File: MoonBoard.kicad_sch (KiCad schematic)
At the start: 48 parts, among them SW1 SW_SPST, SW2 SW_DIP_x04, U1 AMS1117-3.3, U2 74LS08, U3 STM32F303CBTx, U5 H5VU25U, Y1 16MHz

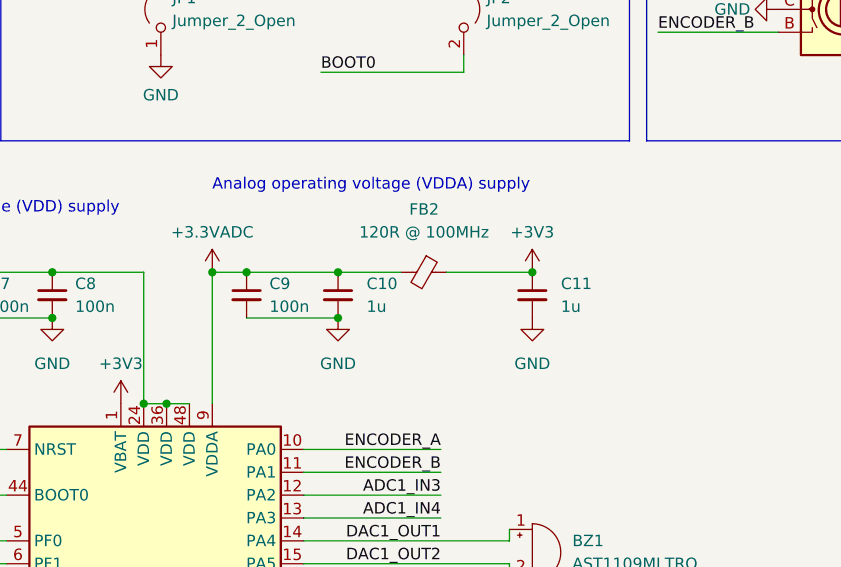
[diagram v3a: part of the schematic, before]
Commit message: make VDDA ~2V
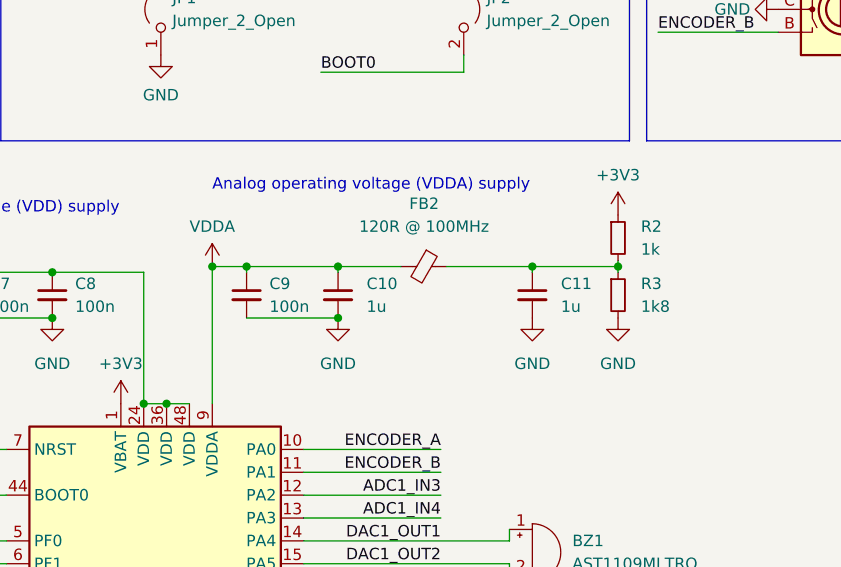
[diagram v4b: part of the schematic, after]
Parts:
- added R2: 1k, Resistor_SMD:R_0402_1005Metric, symbol Device:R_Small
- added R3: 1k8, Resistor_SMD:R_0402_1005Metric, symbol Device:R_Small
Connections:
- net +3V3: now also R2.1; no longer C11.1, FB2.1
- net GND: now also R3.2
- net +3.3VADC renamed VDDA
- new net: C11.1, FB2.1, R2.2, R3.1
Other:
- moved on the sheet: FB2

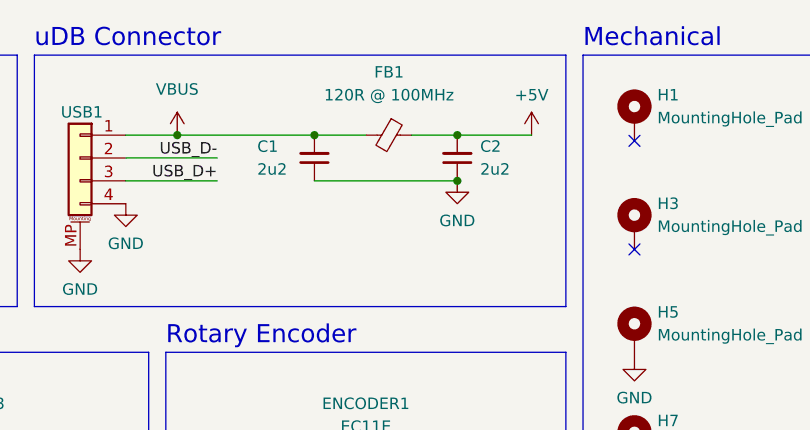
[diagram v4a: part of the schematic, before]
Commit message: new board outline remove VBUS PI filter
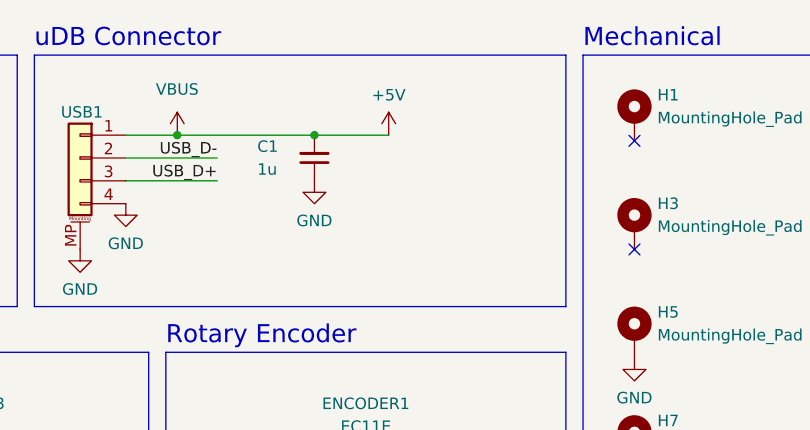
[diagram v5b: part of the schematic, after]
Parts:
- removed C2: 2u2, Capacitor_SMD:C_0805_2012Metric, symbol Device:C_Small
- removed FB1: 120R @ 100MHz, Inductor_SMD:L_0805_2012Metric, symbol Device:FerriteBead_Small
- C1: value 2u2 -> 1u; footprint Capacitor_SMD:C_0805_2012Metric -> Capacitor_SMD:C_0402_1005Metric
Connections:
- net VBUS is gone; now on net +5V: C1.2, USB1.1 (Pin_1)
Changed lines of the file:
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@@
   (junction (at 155.575 26.67) (diameter 0) (color 0 0 0 0)
   )
-  (junction (at 186.69 31.75) (diameter 0) (color 0 0 0 0)
-  )
   (junction (at 17.145 146.05) (diameter 0) (color 0 0 0 0)
   )
@@
   (junction (at 109.855 94.615) (diameter 0) (color 0 0 0 0)
   )
-  (junction (at 186.69 26.67) (diameter 0) (color 0 0 0 0)
-  )
   (junction (at 98.425 109.855) (diameter 0) (color 0 0 0 0)
   )
   (junction (at 318.77 169.545) (diameter 0) (color 0 0 0 0)
   )
+  (junction (at 274.32 139.065) (diameter 0) (color 0 0 0 0)
+  )
+  (junction (at 322.58 120.65) (diameter 0) (color 0 0 0 0)
+  )
+  (junction (at 274.32 141.605) (diameter 0) (color 0 0 0 0)
+  )
+  (junction (at 17.78 27.94) (diameter 0) (color 0 0 0 0)
+  )
+  (junction (at 100.965 109.855) (diameter 0) (color 0 0 0 0)
+  )
+  (junction (at 78.74 95.25) (diameter 0) (color 0 0 0 0)
+  )
+  (junction (at 274.32 136.525) (diameter 0) (color 0 0 0 0)
+  )
+  (junction (at 64.77 111.125) (diameter 0) (color 0 0 0 0)
+  )
+  (junction (at 160.02 149.86) (diameter 0) (color 0 0 0 0)
+  )
+  (junction (at 134.62 145.415) (diameter 0) (color 0 0 0 0)
+  )
+  (junction (at 336.55 113.03) (diameter 0) (color 0 0 0 0)
+  )
+  (junction (at 43.18 27.94) (diameter 0) (color 0 0 0 0)
+  )
+  (junction (at 38.735 135.255) (diameter 0) (color 0 0 0 0)
+  )
   (junction (at 170.815 26.67) (diameter 0) (color 0 0 0 0)
-  )
-  (junction (at 274.32 139.065) (diameter 0) (color 0 0 0 0)
-  )
-  (junction (at 322.58 120.65) (diameter 0) (color 0 0 0 0)
-  )
-  (junction (at 274.32 141.605) (diameter 0) (color 0 0 0 0)
-  )
-  (junction (at 17.78 27.94) (diameter 0) (color 0 0 0 0)
-  )
-  (junction (at 100.965 109.855) (diameter 0) (color 0 0 0 0)
-  )
-  (junction (at 78.74 95.25) (diameter 0) (color 0 0 0 0)
-  )
-  (junction (at 274.32 136.525) (diameter 0) (color 0 0 0 0)
-  )
-  (junction (at 64.77 111.125) (diameter 0) (color 0 0 0 0)
-  )
-  (junction (at 160.02 149.86) (diameter 0) (color 0 0 0 0)
-  )
-  (junction (at 134.62 145.415) (diameter 0) (color 0 0 0 0)
-  )
-  (junction (at 336.55 113.03) (diameter 0) (color 0 0 0 0)
-  )
-  (junction (at 43.18 27.94) (diameter 0) (color 0 0 0 0)
-  )
-  (junction (at 38.735 135.255) (diameter 0) (color 0 0 0 0)
   )
   (junction (at 106.045 94.615) (diameter 0) (color 0 0 0 0)
@@
     (stroke (width 0) (type default))
   )
-  (wire (pts (xy 186.69 26.67) (xy 181.61 26.67))
-    (stroke (width 0) (type default))
-  )
   (wire (pts (xy 57.785 170.815) (xy 83.185 170.815))
     (stroke (width 0) (type default))
@@
     (stroke (width 0) (type default))
   )
-  (wire (pts (xy 176.53 26.67) (xy 170.815 26.67))
-    (stroke (width 0) (type default))
-  )
   (wire (pts (xy 17.145 146.05) (xy 28.575 146.05))
     (stroke (width 0) (type default))
@@
     (stroke (width 0) (type default))
   )
-  (wire (pts (xy 186.69 26.67) (xy 194.945 26.67))
+  (wire (pts (xy 170.815 26.67) (xy 179.07 26.67))
     (stroke (width 0) (type default))
   )
@@
   )
   (wire (pts (xy 97.155 31.75) (xy 87.63 31.75))
-    (stroke (width 0) (type default))
-  )
-  (wire (pts (xy 170.815 31.75) (xy 186.69 31.75))
     (stroke (width 0) (type default))
   )
@@
     )
   )
-  (symbol (lib_id "Device:C_Small") (at 186.69 29.21 180) (unit 1)
-    (in_bom yes) (on_board yes) (dnp no) (fields_autoplaced)
-    (property "Reference" "C2" (at 189.23 27.9336 0)
-      (effects (font (size 1.27 1.27)) (justify right))
-    )
-    (property "Value" "2u2" (at 189.23 30.4736 0)
-      (effects (font (size 1.27 1.27)) (justify right))
-    )
-    (property "Footprint" "Capacitor_SMD:C_0805_2012Metric" (at 186.69 29.21 0)
-      (effects (font (size 1.27 1.27)) hide)
-    )
-    (property "Datasheet" "~" (at 186.69 29.21 0)
-      (effects (font (size 1.27 1.27)) hide)
-    )
-    (pin "1")
-    (pin "2")
-    (instances
-      (project "MoonBoard"
-        (path "/bb706f4b-6d11-4e29-ae30-1a1ffddaf9f4"
-          (reference "C2") (unit 1)
-        )
-      )
-    )
-  )
-  (symbol (lib_id "Device:FerriteBead_Small") (at 179.07 26.67 270) (unit 1)
-    (in_bom yes) (on_board yes) (dnp no) (fields_autoplaced)
-    (property "Reference" "FB1" (at 179.1081 19.685 90)
-      (effects (font (size 1.27 1.27)))
-    )
-    (property "Value" "120R @ 100MHz" (at 179.1081 22.225 90)
-      (effects (font (size 1.27 1.27)))
-    )
-    (property "Footprint" "Inductor_SMD:L_0805_2012Metric" (at 179.07 24.892 90)
-      (effects (font (size 1.27 1.27)) hide)
-    )
-    (property "Datasheet" "~" (at 179.07 26.67 0)
-      (effects (font (size 1.27 1.27)) hide)
-    )
-    (pin "1")
-    (pin "2")
-    (instances
-      (project "MoonBoard"
-        (path "/bb706f4b-6d11-4e29-ae30-1a1ffddaf9f4"
-          (reference "FB1") (unit 1)
-        )
-      )
-    )
-  )
   (symbol (lib_id "Mechanical:MountingHole_Pad") (at 233.045 48.895 0) (unit 1)
     (in_bom no) (on_board yes) (dnp no) (fields_autoplaced)
@@
     )
   )
-  (symbol (lib_id "power:GND") (at 186.69 31.75 0) (mirror y) (unit 1)
-    (in_bom yes) (on_board yes) (dnp no) (fields_autoplaced)
-    (property "Reference" "#PWR06" (at 186.69 38.1 0)
-      (effects (font (size 1.27 1.27)) hide)
-    )
-    (property "Value" "GND" (at 186.69 36.195 0)
-      (effects (font (size 1.27 1.27)))
-    )
-    (property "Footprint" "" (at 186.69 31.75 0)
-      (effects (font (size 1.27 1.27)) hide)
-    )
-    (property "Datasheet" "" (at 186.69 31.75 0)
-      (effects (font (size 1.27 1.27)) hide)
-    )
-    (pin "1")
-    (instances
-      (project "MoonBoard"
-        (path "/bb706f4b-6d11-4e29-ae30-1a1ffddaf9f4"
-          (reference "#PWR06") (unit 1)
-        )
-      )
-    )
-  )
   (symbol (lib_id "Mechanical:MountingHole_Pad") (at 233.045 24.765 0) (unit 1)
     (in_bom no) (on_board yes) (dnp no) (fields_autoplaced)
@@
       (effects (font (size 1.27 1.27)) (justify right))
     )
-    (property "Value" "2u2" (at 164.465 30.48 0)
+    (property "Value" "1u" (at 164.465 30.48 0)
       (effects (font (size 1.27 1.27)) (justify right))
     )
-    (property "Footprint" "Capacitor_SMD:C_0805_2012Metric" (at 170.815 29.21 0)
+    (property "Footprint" "Capacitor_SMD:C_0402_1005Metric" (at 170.815 29.21 0)
       (effects (font (size 1.27 1.27)) hide)
     )
@@
     )
   )
-  (symbol (lib_id "power:+5V") (at 194.945 26.67 0) (mirror y) (unit 1)
-    (in_bom yes) (on_board yes) (dnp no) (fields_autoplaced)
-    (property "Reference" "#PWR04" (at 194.945 30.48 0)
-      (effects (font (size 1.27 1.27)) hide)
-    )
-    (property "Value" "+5V" (at 194.945 22.225 0)
-      (effects (font (size 1.27 1.27)))
-    )
-    (property "Footprint" "" (at 194.945 26.67 0)
-      (effects (font (size 1.27 1.27)) hide)
-    )
-    (property "Datasheet" "" (at 194.945 26.67 0)
+  (symbol (lib_id "power:+5V") (at 179.07 26.67 0) (mirror y) (unit 1)
+    (in_bom yes) (on_board yes) (dnp no) (fields_autoplaced)
+    (property "Reference" "#PWR04" (at 179.07 30.48 0)
+      (effects (font (size 1.27 1.27)) hide)
+    )
+    (property "Value" "+5V" (at 179.07 22.225 0)
+      (effects (font (size 1.27 1.27)))
+    )
+    (property "Footprint" "" (at 179.07 26.67 0)
+      (effects (font (size 1.27 1.27)) hide)
+    )
+    (property "Datasheet" "" (at 179.07 26.67 0)
       (effects (font (size 1.27 1.27)) hide)
     )
@@
         )
       )
+    )
+  )
+  (symbol (lib_id "power:GND") (at 170.815 31.75 0) (mirror y) (unit 1)
+    (in_bom yes) (on_board yes) (dnp no) (fields_autoplaced)
+    (property "Reference" "#PWR06" (at 170.815 38.1 0)
+      (effects (font (size 1.27 1.27)) hide)
+    )
+    (property "Value" "GND" (at 170.815 36.195 0)
+      (effects (font (size 1.27 1.27)))
+    )
+    (property "Footprint" "" (at 170.815 31.75 0)
+      (effects (font (size 1.27 1.27)) hide)
+    )
+    (property "Datasheet" "" (at 170.815 31.75 0)
+      (effects (font (size 1.27 1.27)) hide)
+    )
+    (pin "1")
+    (instances
+      (project "MoonBoard"
+        (path "/bb706f4b-6d11-4e29-ae30-1a1ffddaf9f4"
+          (reference "#PWR06") (unit 1)
+        )
+      )

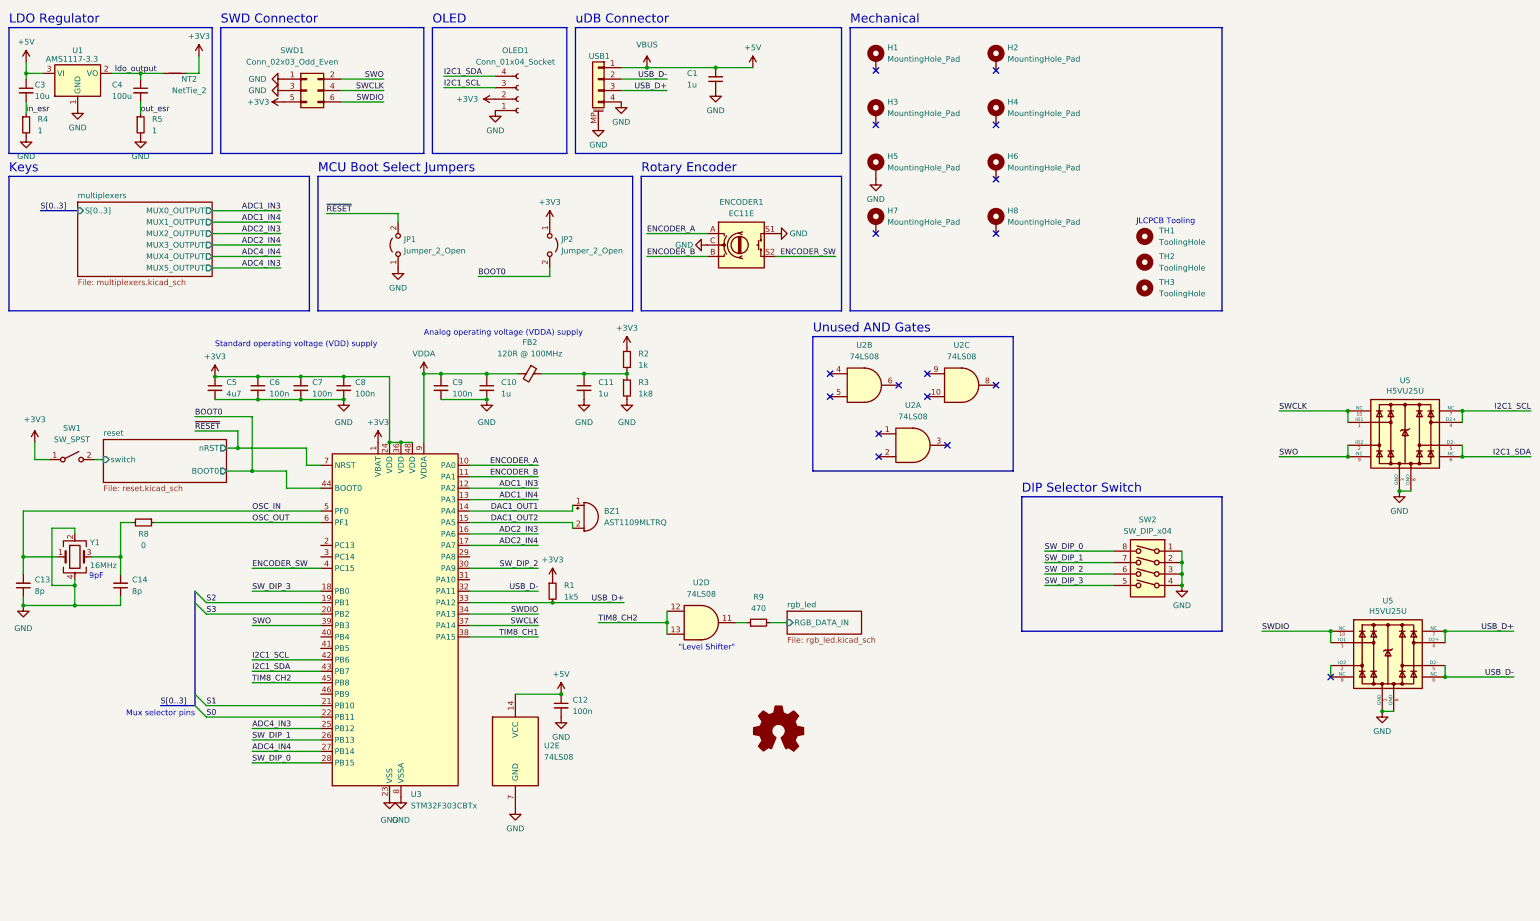
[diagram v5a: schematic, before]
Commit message: add 0R usb termination resistors change muxes to 3V3
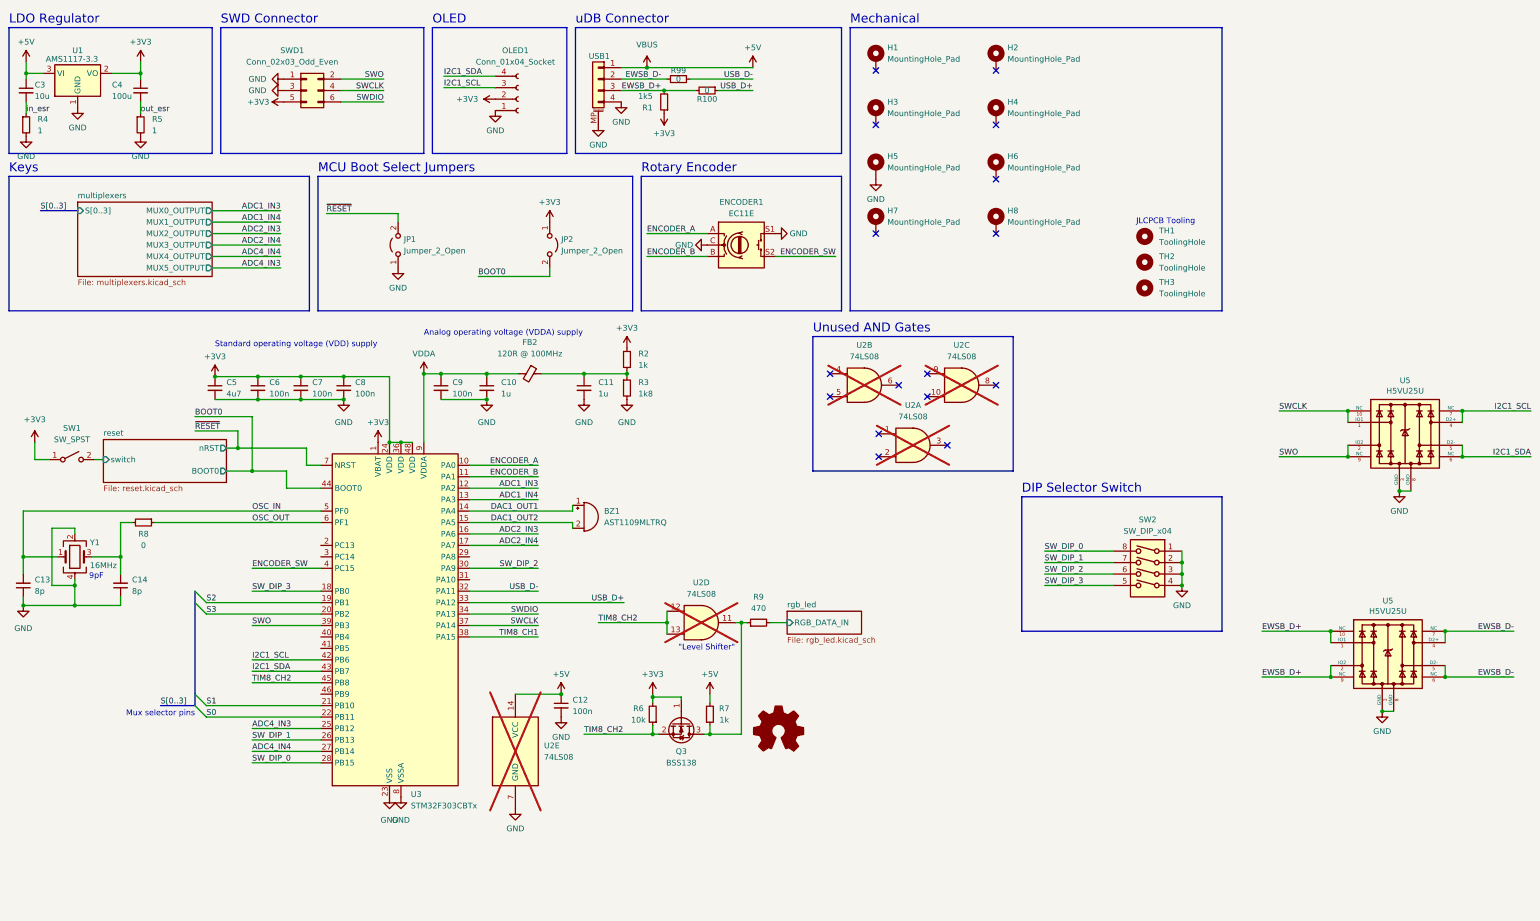
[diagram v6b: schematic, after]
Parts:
- removed C1: 1u, Capacitor_SMD:C_0402_1005Metric, symbol Device:C_Small
- removed NT2: NetTie_2, NetTie:NetTie-2_SMD_Pad0.5mm, symbol Device:NetTie_2
- added Q3: BSS138, Package_TO_SOT_SMD:SOT-23, symbol Transistor_FET:BSS138
- added R100, R99: 0, Resistor_SMD:R_0603_1608Metric_Pad0.98x0.95mm_HandSolder, symbol Device:R_Small
- added R6: 10k, Resistor_SMD:R_0402_1005Metric, symbol Device:R_Small
- added R7: 1k, Resistor_SMD:R_0402_1005Metric, symbol Device:R_Small
- U2: now not fitted
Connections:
- net ldo_output is gone; now on net +3V3: C4.1, U1.2 (VO)
- net +3V3: now also Q3.1 (G), R6.2
- net +5V: now also R7.2
- net SWDIO: no longer U5.1 (IO1), U5.10 (NC)
- net TIM8_CH2: now also Q3.2 (S), R6.1
- net USB_D+: now also R100.1; no longer R1.2, U5.4 (D2+), U5.7 (NC), USB1.3 (Pin_3)
- net USB_D-: now also R99.1; no longer U5.5 (D2-), U5.6 (NC), USB1.2 (Pin_2)
- net EWSB_D+: now reaches U5.2 (IO2), U5.9 (NC)
- net EWSB_D+: now also R1.2, U5.1 (IO1), U5.10 (NC), USB1.3 (Pin_3), R100.2
- net at R9.1, U2.11: now also Q3.3 (D), R7.1
- new net EWSB_D-: R99.2, U5.4 (D2+), U5.5 (D2-), U5.6 (NC), U5.7 (NC), USB1.2 (Pin_2)
- no-connect marks 17 -> 16
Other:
- moved on the sheet: R1
